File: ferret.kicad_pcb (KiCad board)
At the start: 4 copper layers, 50 x 50 mm, 132 parts, among them J201 Power, J301 BAT, J302 BAT, J303 SYS, J401 CHG, J402 CTRL, J403 SOICbite, J404 RS485, Q201 40V, Q202 40V, Q203 40V, SW201 Dead Battery, SW401 RESET, SW402 USER, U201 TPD6S300A, U202 FUSB307BMPX, U203 FSUSB42MUX, U301 TPS560430X3F, U302 BQ25792, U401 STM32F072CBTx, U402 CH340G, U403 SP3485EN, Y401 12MHz

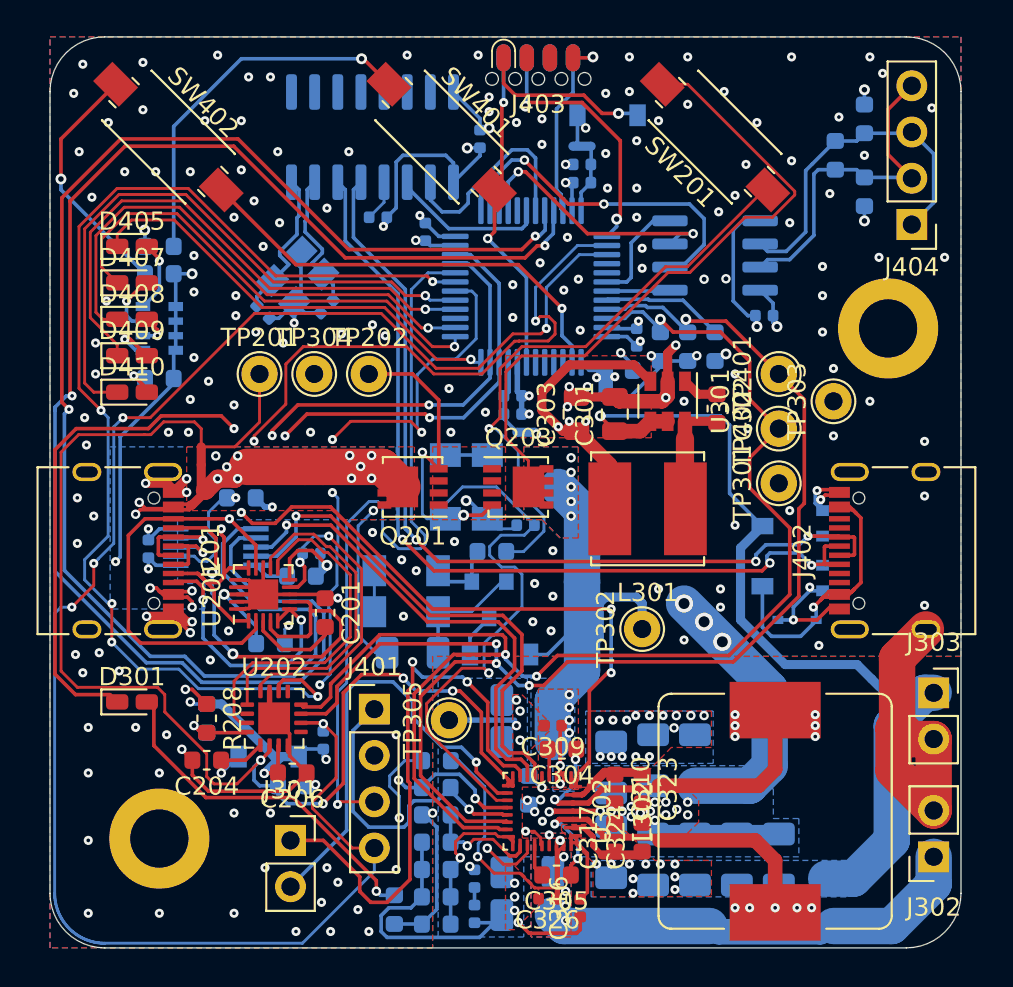
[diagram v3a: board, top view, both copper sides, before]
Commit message: Fix silkscreen, still needs some sillyness
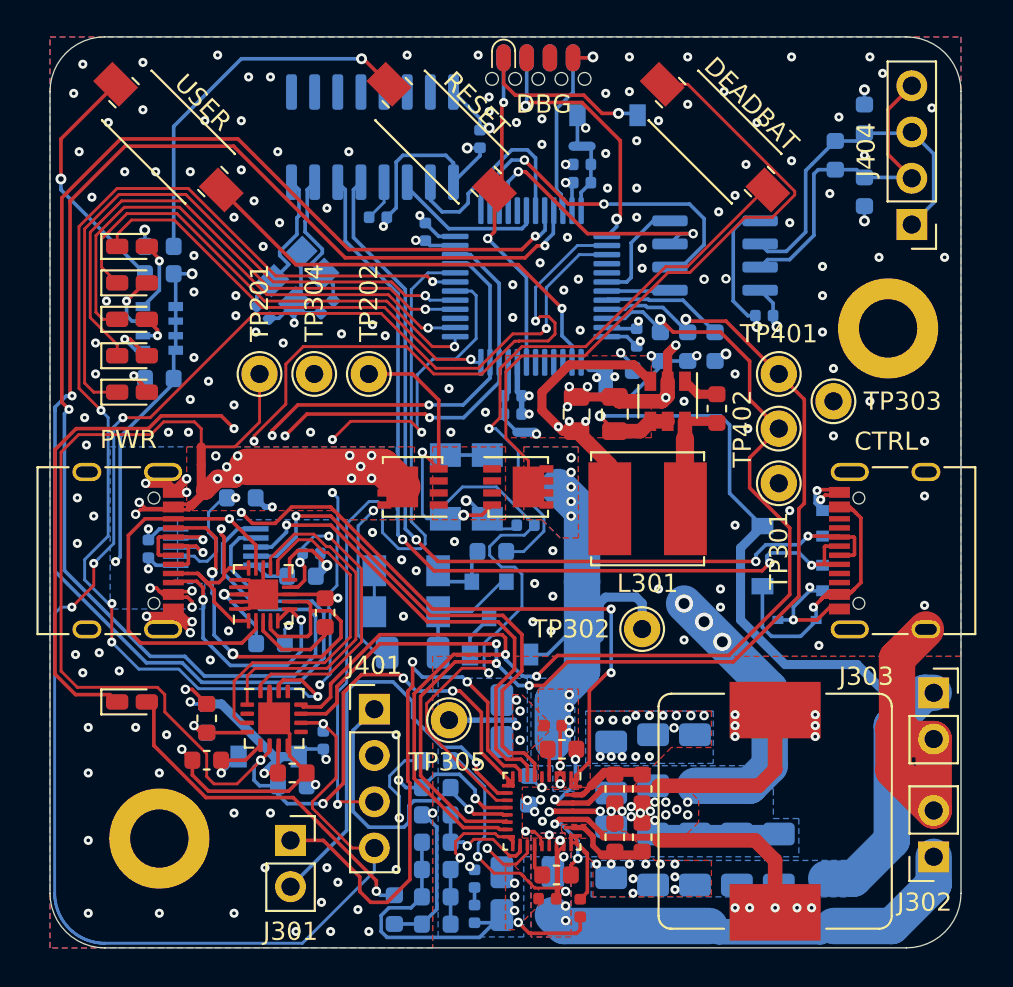
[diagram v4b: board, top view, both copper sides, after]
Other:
- board text added: "CTRL"
- board text added: "DBG"
- board text added: "DEADBAT"
- board text added: "PWR"
- board text added: "RESET"
- board text added: "USER"

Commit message: Add a few more PNs, change D401 to a standard part
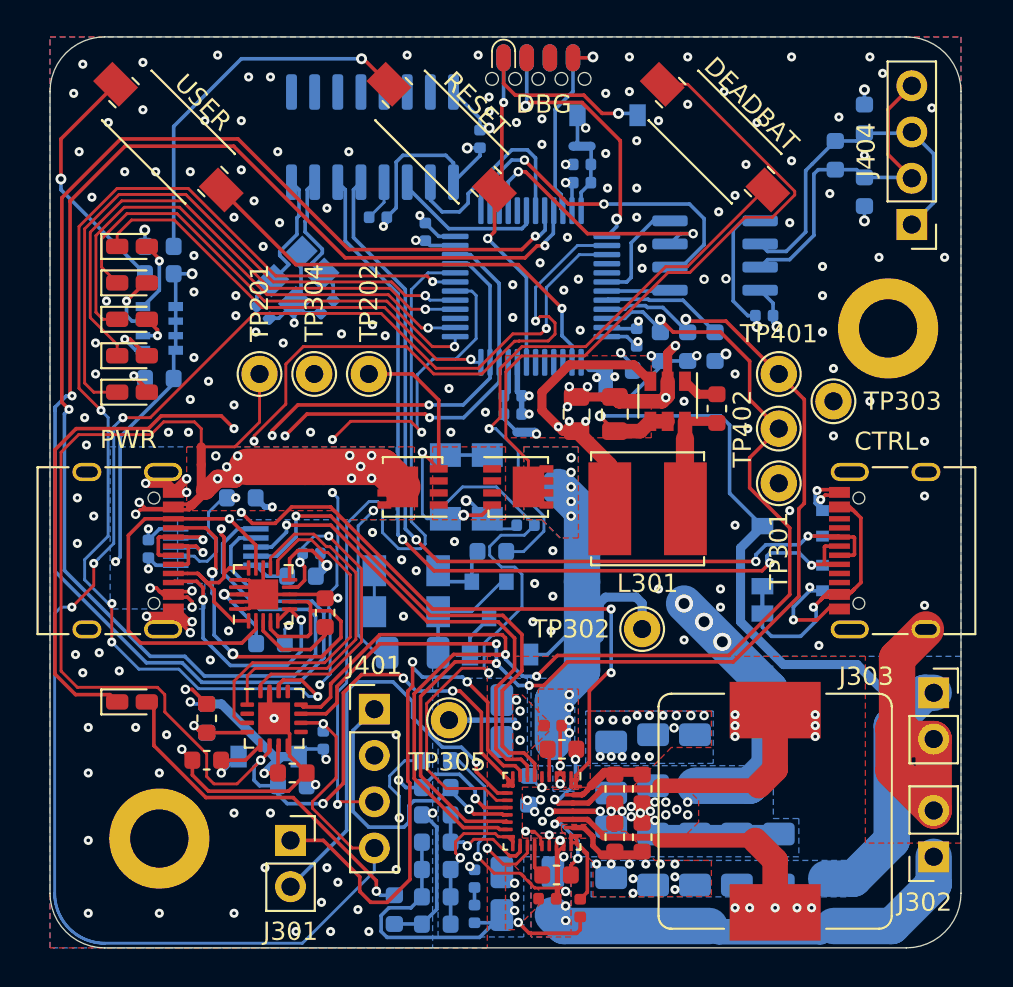
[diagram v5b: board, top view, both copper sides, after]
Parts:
- D401: footprint Diode_SMD:D_SOD-323 -> Diode_SMD:D_SOD-123
- moved D401 2.30 mm to (163.1, 121.3), turned to 270 degrees
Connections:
- J402 pad A5: Net-(J402-PadA5) -> (no net)
- J402 pad A8: Net-(J402-PadA8) -> (no net)
- J402 pad B5: Net-(J402-PadB5) -> (no net)
- J402 pad B8: Net-(J402-PadB8) -> (no net)
- J403 pad 2: Net-(J403-Pad2) -> (no net)
- J403 pad 3: Net-(J403-Pad3) -> (no net)
- J403 pad 6: Net-(J403-Pad6) -> (no net)
- U202 pad 13: Net-(U202-Pad13) -> (no net)
- U202 pad 2: Net-(U202-Pad2) -> (no net)
- U202 pad 9: Net-(U202-Pad9) -> (no net)
- U401 pad 15: Net-(U401-Pad15) -> (no net)
- U401 pad 26: /Control/EXT_SCL -> (no net)
- U401 pad 27: /Control/EXT_SDA -> (no net)
- U401 pad 29: Net-(U401-Pad29) -> (no net)
- U401 pad 3: Net-(U401-Pad3) -> (no net)
- U401 pad 4: Net-(U401-Pad4) -> (no net)
- U401 pad 40: Net-(U401-Pad40) -> (no net)
- U401 pad 41: Net-(U401-Pad41) -> (no net)
- U401 pad 5: Net-(U401-Pad5) -> (no net)
- U401 pad 6: Net-(U401-Pad6) -> (no net)
- U402 pad 10: Net-(U402-Pad10) -> (no net)
- U402 pad 11: Net-(U402-Pad11) -> (no net)
- U402 pad 12: Net-(U402-Pad12) -> (no net)
- U402 pad 13: Net-(U402-Pad13) -> (no net)
- U402 pad 14: Net-(U402-Pad14) -> (no net)
- U402 pad 15: Net-(U402-Pad15) -> (no net)
- U402 pad 9: Net-(U402-Pad9) -> (no net)
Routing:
- net Net-(D401-Pad1): track 18.1 -> 19.6 mm
- net /Input Side/ACDRV1: track 48.0 -> 49.2 mm
- net GND: track 134.5 -> 133.6 mm, vias 191 -> 192

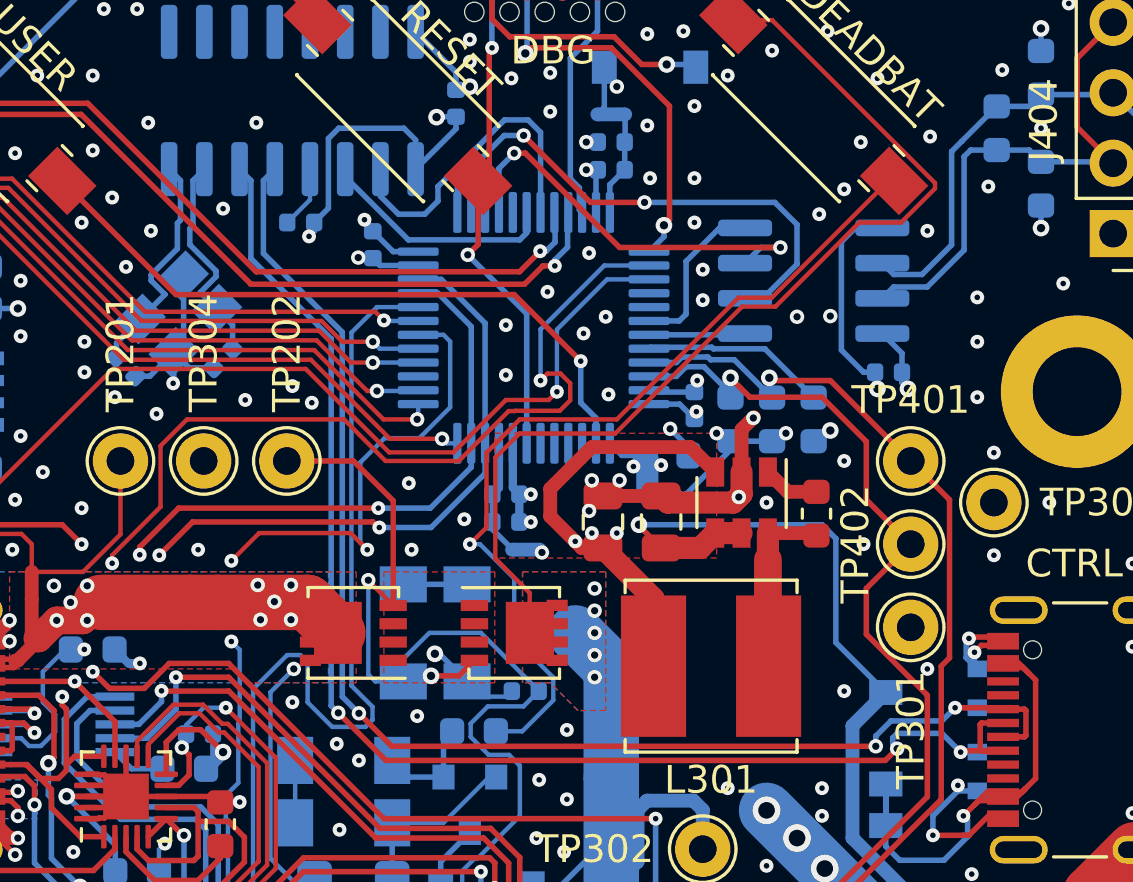
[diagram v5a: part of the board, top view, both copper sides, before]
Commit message: added a crystal
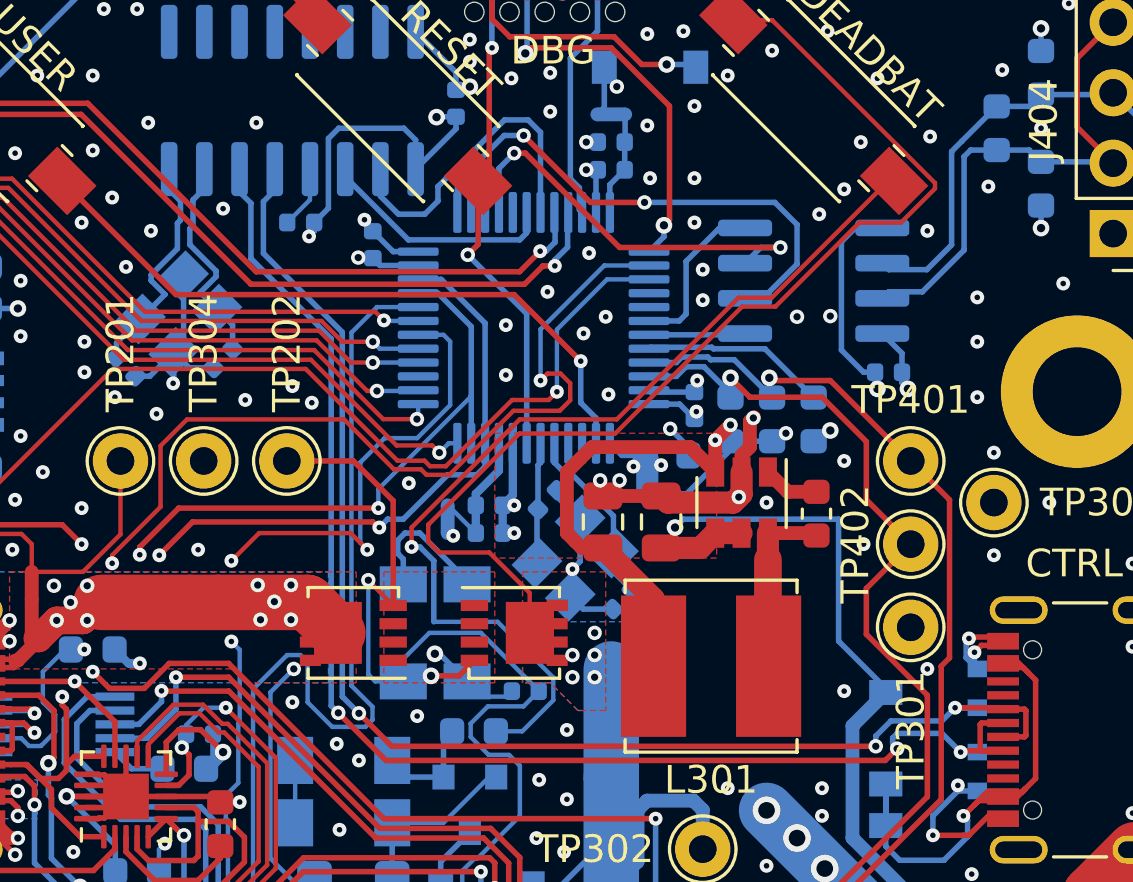
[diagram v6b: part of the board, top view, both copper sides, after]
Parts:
- added C413: 12pF, Capacitor_SMD:C_0402_1005Metric, B.Cu at (153.6, 111.5)
- added C414: 12pF, Capacitor_SMD:C_0402_1005Metric, B.Cu at (150.9, 107.9)
- added Y402: 12MHz, Crystal:Crystal_SMD_3225-4Pin_3.2x2.5mm, B.Cu at (151.9, 110.0)
- moved NT401 3.03 mm to (147.3, 108.6), turned to 90 degrees
- moved C411 0.72 mm to (148.8, 109.1)
- moved C412 0.72 mm to (148.8, 108.1)
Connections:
- J402 pad A5: (no net) -> Net-(J402-PadA5)
- J402 pad A8: (no net) -> Net-(J402-PadA8)
- J402 pad B5: (no net) -> Net-(J402-PadB5)
- J402 pad B8: (no net) -> Net-(J402-PadB8)
- J403 pad 2: (no net) -> Net-(J403-Pad2)
- J403 pad 3: (no net) -> Net-(J403-Pad3)
- J403 pad 6: (no net) -> Net-(J403-Pad6)
- U202 pad 13: (no net) -> Net-(U202-Pad13)
- U202 pad 2: (no net) -> Net-(U202-Pad2)
- U202 pad 9: (no net) -> Net-(U202-Pad9)
- U401 pad 15: (no net) -> Net-(U401-Pad15)
- U401 pad 26: (no net) -> /Control/EXT_SCL
- U401 pad 27: (no net) -> /Control/EXT_SDA
- U401 pad 29: (no net) -> Net-(U401-Pad29)
- U401 pad 3: (no net) -> Net-(U401-Pad3)
- U401 pad 4: (no net) -> Net-(U401-Pad4)
- U401 pad 40: (no net) -> Net-(U401-Pad40)
- U401 pad 41: (no net) -> Net-(U401-Pad41)
- U401 pad 5: (no net) -> /Control/MCUXT_N
- U401 pad 6: (no net) -> /Control/MCUXT_P
- U402 pad 10: (no net) -> Net-(U402-Pad10)
- U402 pad 11: (no net) -> Net-(U402-Pad11)
- U402 pad 12: (no net) -> Net-(U402-Pad12)
- U402 pad 13: (no net) -> Net-(U402-Pad13)
- U402 pad 14: (no net) -> Net-(U402-Pad14)
- U402 pad 15: (no net) -> Net-(U402-Pad15)
- U402 pad 9: (no net) -> Net-(U402-Pad9)
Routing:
- net /Control/MCUXT_N: track 0.00 -> 6.57 mm
- net GND: track 133.6 -> 139.3 mm, vias 192 -> 190
- net /Control/MCUXT_P: track 0.00 -> 4.37 mm
- net Net-(R202-Pad1): track 31.9 -> 35.0 mm
- net Net-(D203-Pad2): track 2.30 -> 5.13 mm
- net VBUS: track 48.1 -> 49.3 mm
- net VCC: track 33.4 -> 32.5 mm
- net /Control/VDDA: track 4.20 -> 5.01 mm
- net +3V3: track 97.0 -> 97.8 mm, vias 20 -> 18
- net /Control/SBU2: track 49.8 -> 50.4 mm

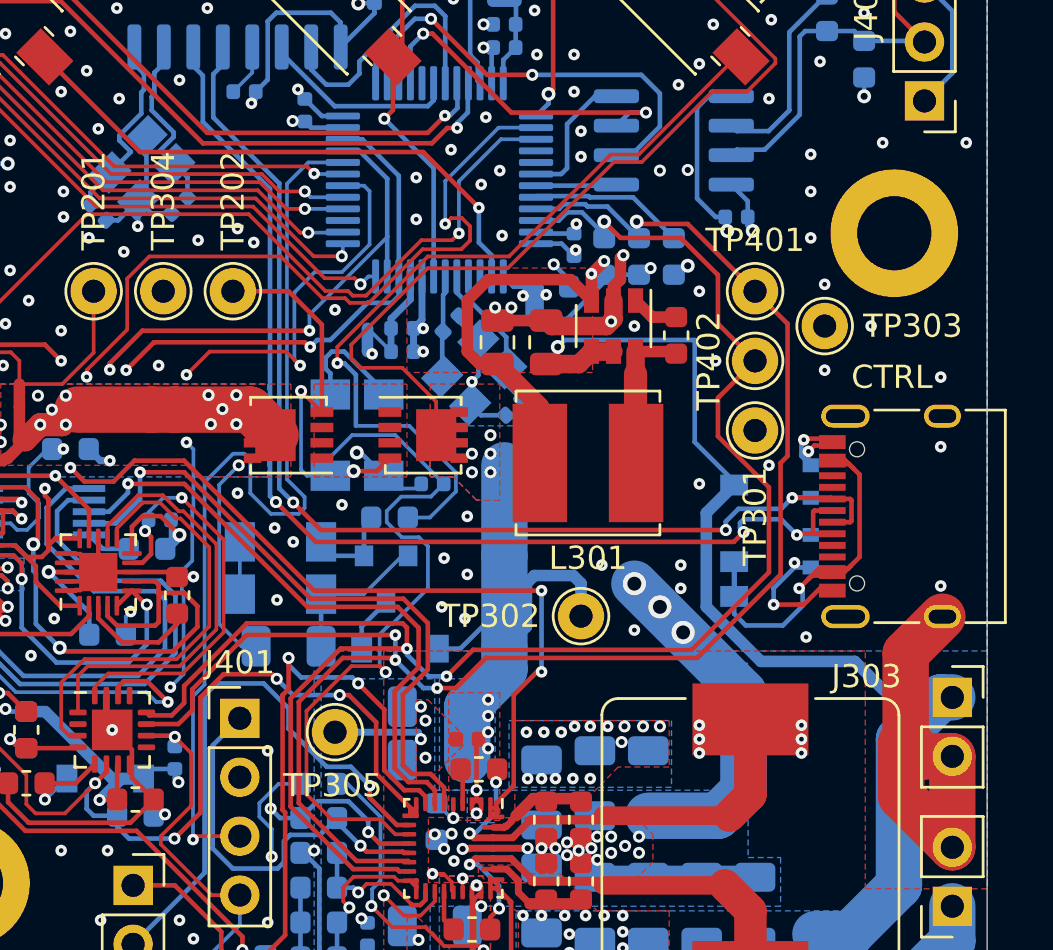
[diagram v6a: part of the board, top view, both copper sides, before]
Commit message: finished routing. no silk artwork.
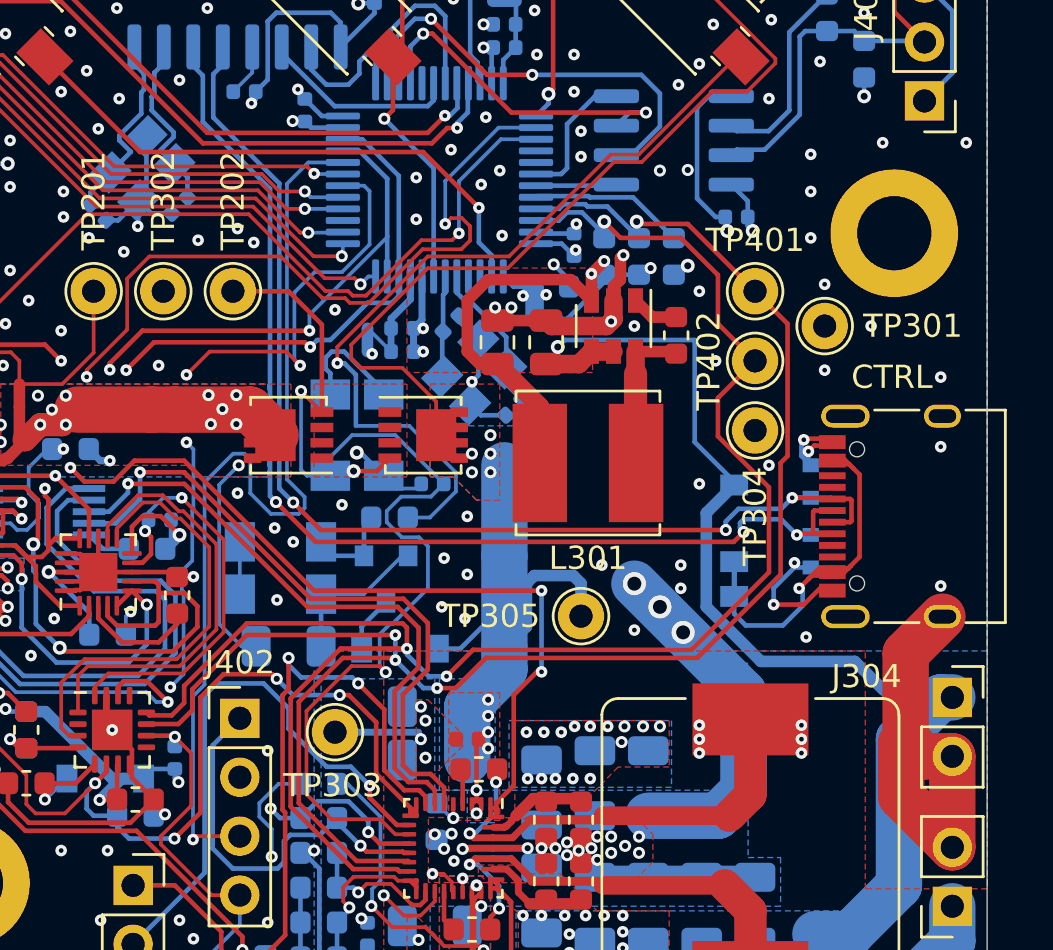
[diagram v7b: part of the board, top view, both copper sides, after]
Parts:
- renumbered C306 to C304, C308 to C305, C309 to C306, C304 to C307, C305 to C308, C307 to C309, C323 to C311, C326 to C312, C311 to C313, C312 to C314, C324 to C315, C313 to C316, C314 to C317, C316 to C318, C317 to C319, C315 to C320, C318 to C321, C319 to C322, C320 to C323, C321 to C324, C322 to C325, C413 to C401, C414 to C402, C401 to C403, C402 to C404, C403 to C405, C404 to C406, C405 to C407, C406 to C408, C407 to C409, C408 to C410, C409 to C411, C410 to C412, C411 to C413, C412 to C414, D206 to D204, D204 to D205, D205 to D206, J303 to J304, J402 to J401, J401 to J402, NT1 to NT201, NT302 to NT301, NT2 to NT302, NT301 to NT303, NT402 to NT401, NT403 to NT402, NT401 to NT403, R308 to R301, R309 to R302, R305 to R303, R306 to R304, R307 to R305, R301 to R306, R302 to R307, R310 to R308, R303 to R309, R304 to R310, R403 to R401, R401 to R402, R402 to R403, R411 to R407, R410 to R408, R412 to R409, R413 to R410, SW402 to SW401, SW401 to SW402, TP303 to TP301, TP304 to TP302, TP305 to TP303, TP301 to TP304, TP302 to TP305, Y402 to Y401, Y401 to Y402
